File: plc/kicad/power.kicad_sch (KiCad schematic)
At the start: 0 parts

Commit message: Added CAN circuit
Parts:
- added F1: BSMD1206C-1300T, LibrePLC32:F1206, symbol LibrePLC32:BSMD1206C-1300T
- added R1: 0, Jumper:SolderJumper-2_P1.3mm_Bridged2Bar_Pad1.0x1.5mm, symbol Device:R
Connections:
- new net +5V: R1.2
- new net +VSYS: F1.1
- new net VBUS: R1.1

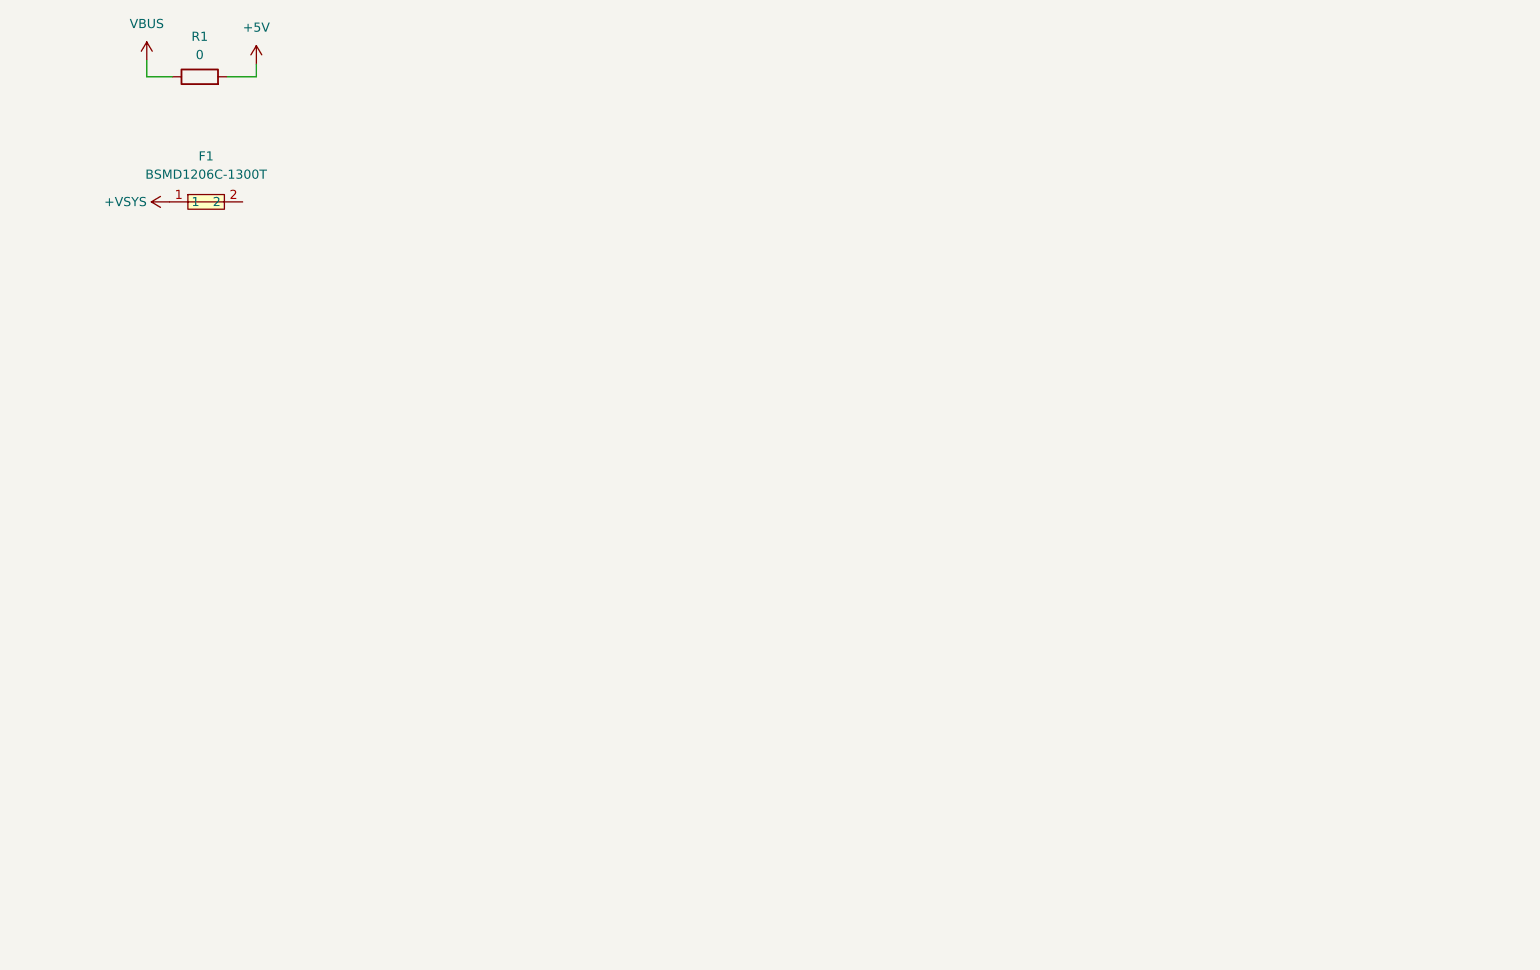
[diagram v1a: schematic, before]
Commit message: Added buck converter circuit
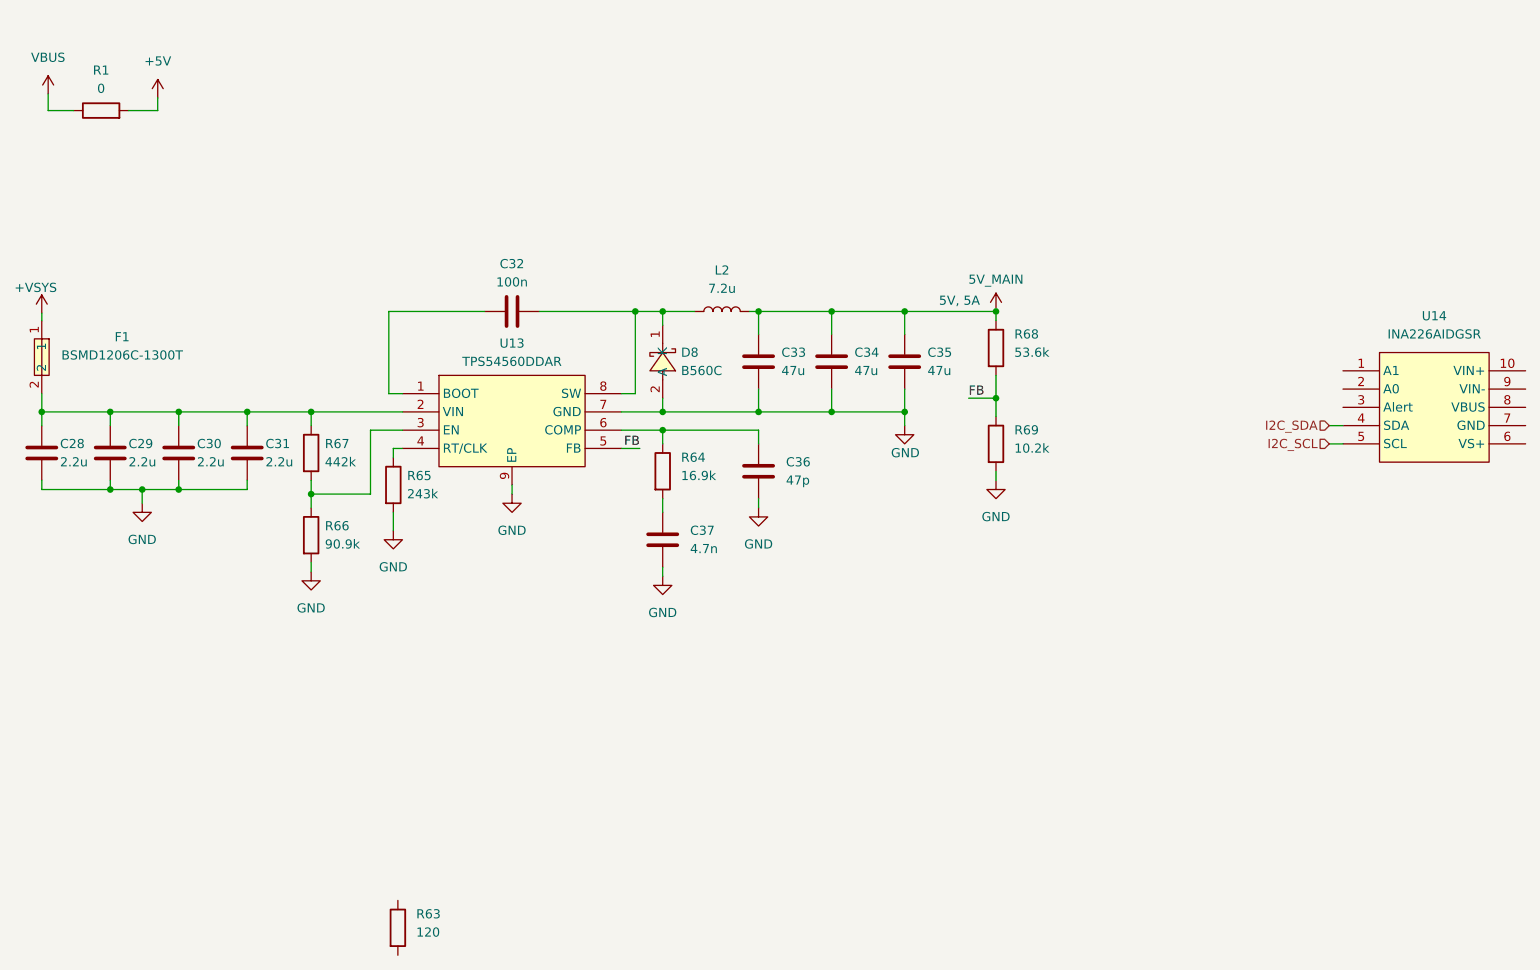
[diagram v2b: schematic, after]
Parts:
- added C28, C29, C30, C31: 2.2u, Capacitor_SMD:C_0805_2012Metric, symbol Device:C
- added C32: 100n, Capacitor_SMD:C_0805_2012Metric, symbol Device:C
- added C33, C34, C35: 47u, Capacitor_SMD:C_0805_2012Metric, symbol Device:C
- added C36: 47p, Capacitor_SMD:C_0805_2012Metric, symbol Device:C
- added C37: 4.7n, Capacitor_SMD:C_0805_2012Metric, symbol Device:C
- added D8: B560C, LibrePLC32:SMC_L6.9-W5.9-LS7.9-RD, symbol LibrePLC32:B560C_C6807784
- added L2: 7.2u, symbol Device:L
- added R63: 120, Resistor_SMD:R_0805_2012Metric, symbol Device:R
- added R64: 16.9k, Resistor_SMD:R_0805_2012Metric, symbol Device:R
- added R65: 243k, Resistor_SMD:R_0805_2012Metric, symbol Device:R
- added R66: 90.9k, Resistor_SMD:R_0805_2012Metric, symbol Device:R
- added R67: 442k, Resistor_SMD:R_0805_2012Metric, symbol Device:R
- added R68: 53.6k, Resistor_SMD:R_0805_2012Metric, symbol Device:R
- added R69: 10.2k, Resistor_SMD:R_0805_2012Metric, symbol Device:R
- added U13: TPS54560DDAR, LibrePLC32:SOIC-8_L5.0-W4.0-P1.27-LS6.0-BL-EP2.0, symbol LibrePLC32:TPS54560DDAR
- added U14: INA226AIDGSR, LibrePLC32:MSOP-10_L3.0-W3.0-P0.50-LS5.0-BL, symbol LibrePLC32:INA226AIDGSR
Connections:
- net at F1.2: now also C28.1, C29.1, C30.1, C31.1, R67.1, U13.2 (VIN)
- new net: C32.1, U13.1 (BOOT)
- new net: R66.1, R67.2, U13.3 (EN)
- new net: R65.1, U13.4 (RT/CLK)
- new net: C36.2, R64.1, U13.6 (COMP)
- new net: C32.2, D8.1 (K), L2.1, U13.8 (SW)
- new net: C37.2, R64.2
- new net 5V_MAIN: C33.2, C34.2, C35.2, L2.2, R68.1
- new net FB: R68.2, R69.1, U13.5 (FB)
- new net GND: C28.2, C29.2, C30.2, C31.2, C33.1, C34.1, C35.1, C36.1, C37.1, D8.2 (A), R65.2, R66.2, R69.2, U13.7 (GND), U13.9 (EP)
- new net I2C_SCL: U14.5 (SCL)
- new net I2C_SDA: U14.4 (SDA)
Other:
- note added: "5V, 5A"
- moved on the sheet: R1

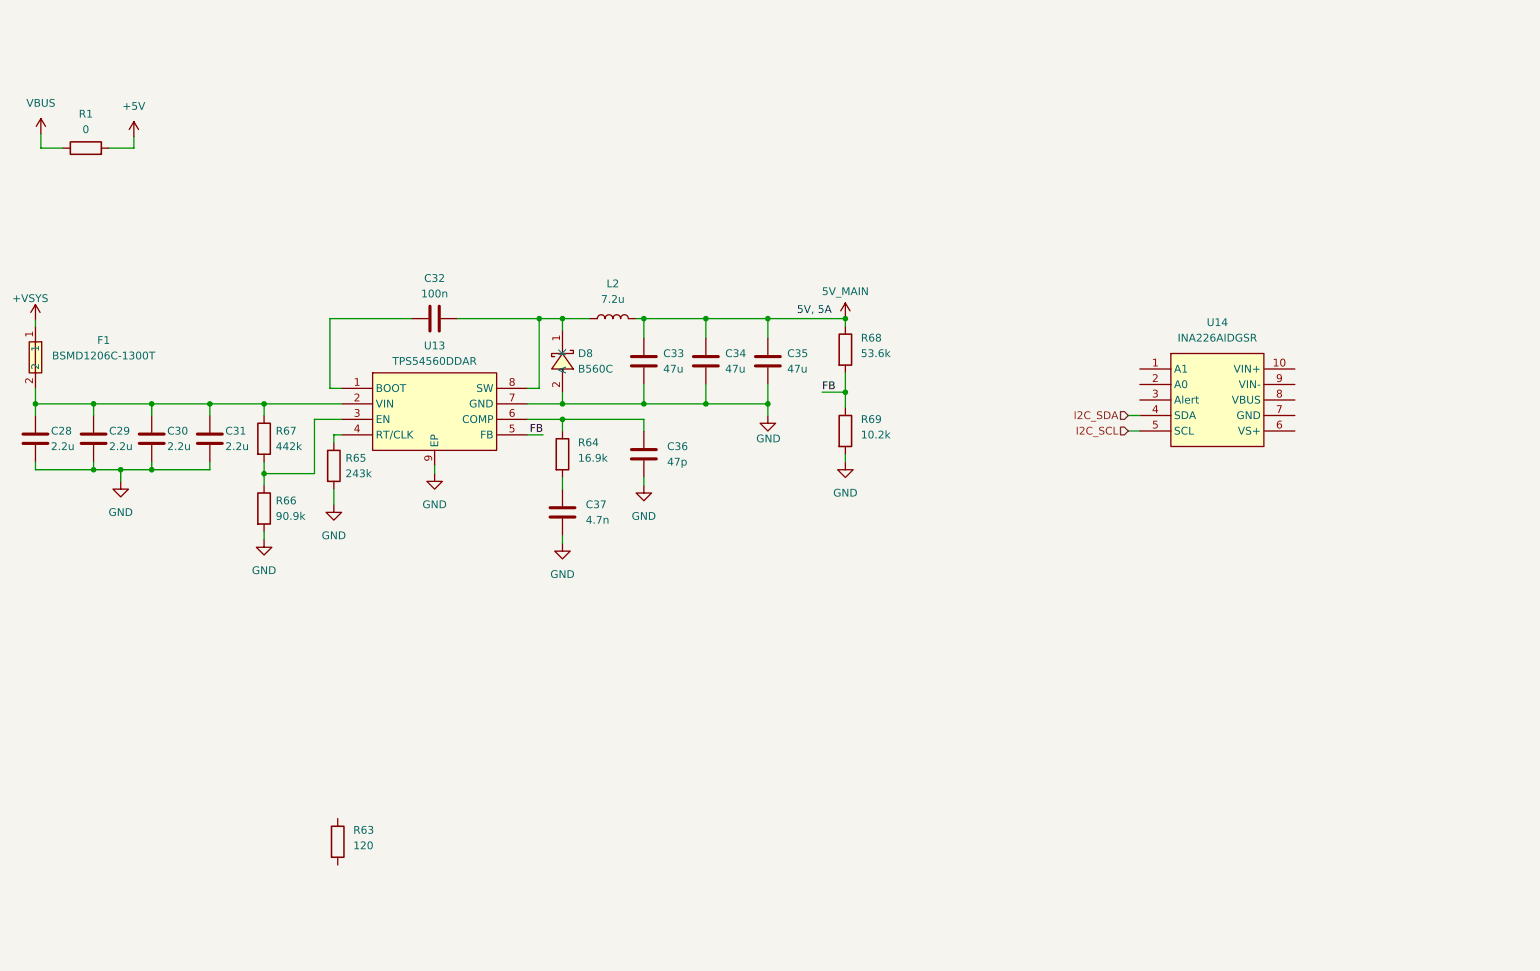
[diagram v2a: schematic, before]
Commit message: Added netclasses
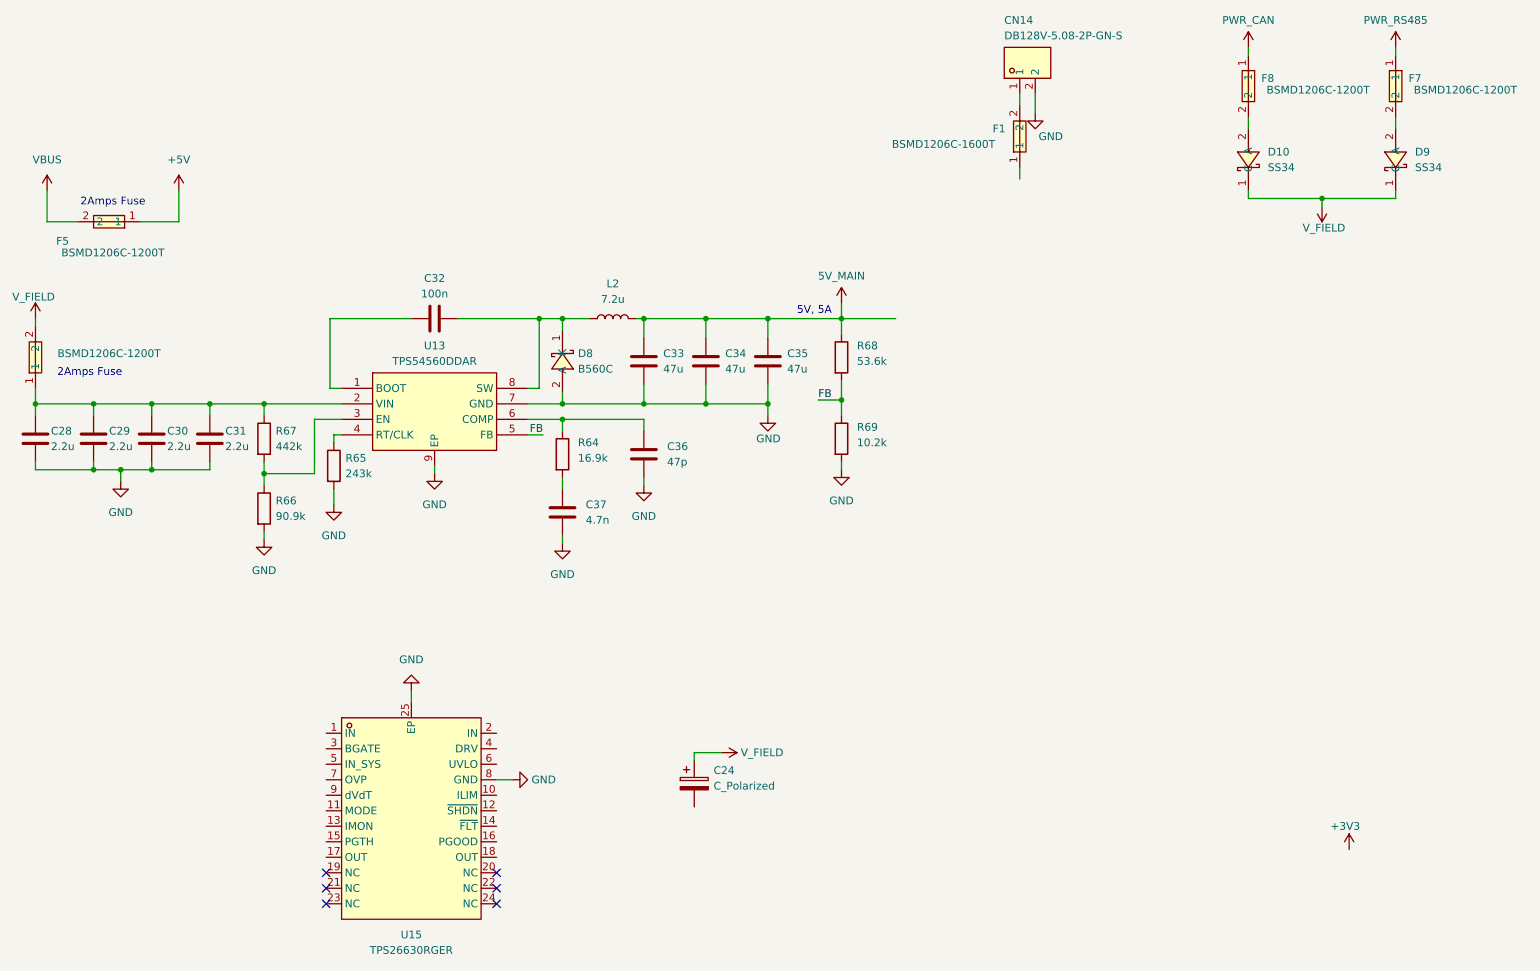
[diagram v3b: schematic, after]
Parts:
- removed F1: BSMD1206C-1300T, LibrePLC32:F1206, symbol LibrePLC32:BSMD1206C-1300T
- removed R1: 0, Jumper:SolderJumper-2_P1.3mm_Bridged2Bar_Pad1.0x1.5mm, symbol Device:R
- removed R63: 120, Resistor_SMD:R_0805_2012Metric, symbol Device:R
- removed U14: INA226AIDGSR, LibrePLC32:MSOP-10_L3.0-W3.0-P0.50-LS5.0-BL, symbol LibrePLC32:INA226AIDGSR
- added C24: C_Polarized, symbol Device:C_Polarized
- added CN14: DB128V-5.08-2P-GN-S, LibrePLC32:CONN-TH_2P-P5.08_DIBO_DB128V-5.08, symbol LibrePLC32:DB128V-5.08-2P-GN-S
- added D10, D9: SS34, LibrePLC32:SMA_L4.3-W2.7-LS5.1-RD, symbol LibrePLC32:SS34_C908680
- added F1: BSMD1206C-1600T, LibrePLC32:F1206, symbol LibrePLC32:BSMD1206C-1600T
- added F5, F6, F7, F8: BSMD1206C-1200T, LibrePLC32:F1206, symbol LibrePLC32:BSMD1206C-1200T
- added U15: TPS26630RGER, LibrePLC32:TQFN-24_L4.0-W4.0-P0.50-TL-EP, symbol LibrePLC32:TPS26630RGER
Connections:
- net +5V: now also F5.1
- net GND: now also CN14.2, U15.25 (EP), U15.8 (GND)
- net VBUS: now also F5.2
- net at C28.1, C29.1, C30.1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: now also F6.1
- new net: D9.2 (A), F7.2
- new net: CN14.1, F1.2
- new net: D10.2 (A), F8.2
- new net PWR_CAN: F8.1
- new net PWR_RS485: F7.1
- new net V_FIELD: C24.1, D10.1 (C), D9.1 (C), F6.2
- no-connect marks 0 -> 6
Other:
- note added: "2Amps Fuse"
